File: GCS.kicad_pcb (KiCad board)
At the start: 2 copper layers, 53 parts, among them J1 PROC_EXTAL_GND, J2 USB_B, J3 PA_CON, J4 PB_CON, J5 ASYNC0_OPT, J6 ASYNC0_IO, J7 ASYNC1_OPT, J8 ASYNC1_IO, SW1 SW_Push, U1 MC6809, U10 MC6850, U11 74HCT00, U2 DS1813, U3 MC68B21, U4 HM62256BLP-7, U5 29C256, U6 74LS138, U7 74LS138, U8 MC6850, U9 74LS138, X1 CXO_DIP8, Y1 Crystal

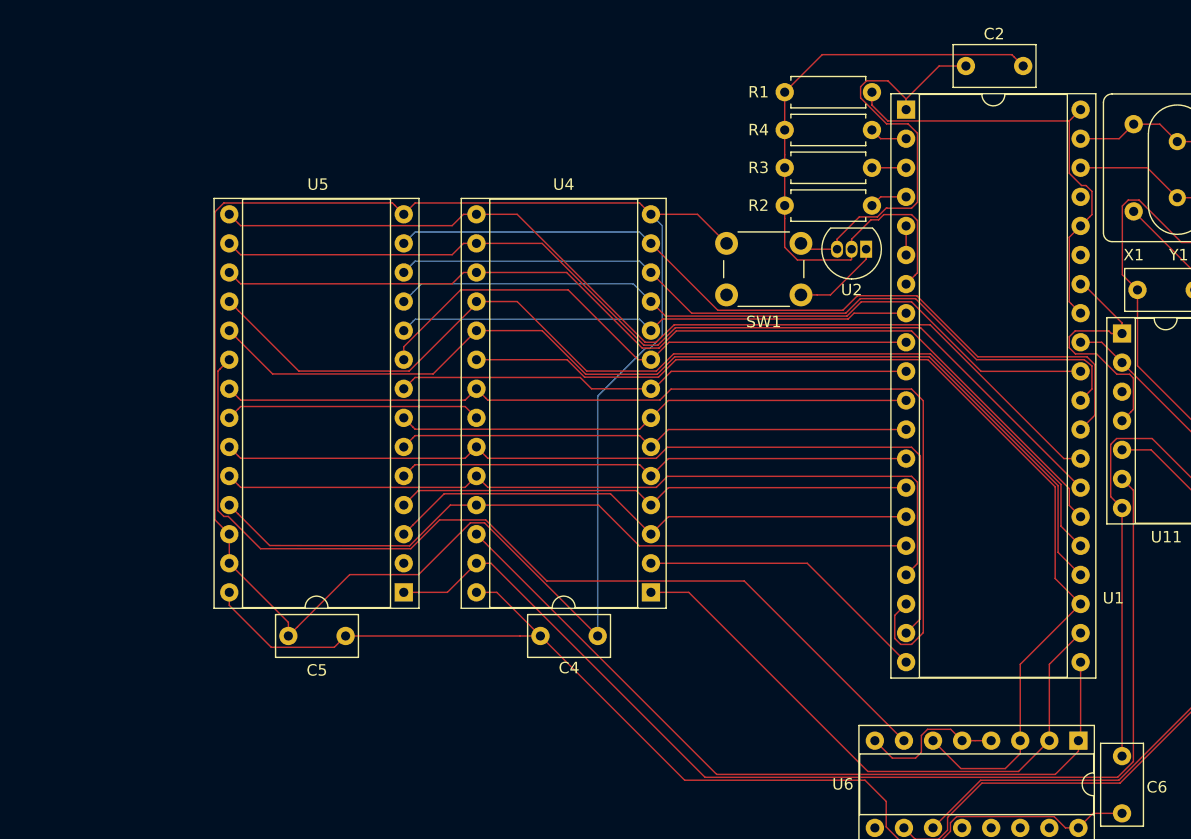
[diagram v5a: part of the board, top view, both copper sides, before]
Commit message: Added header for expandable ram
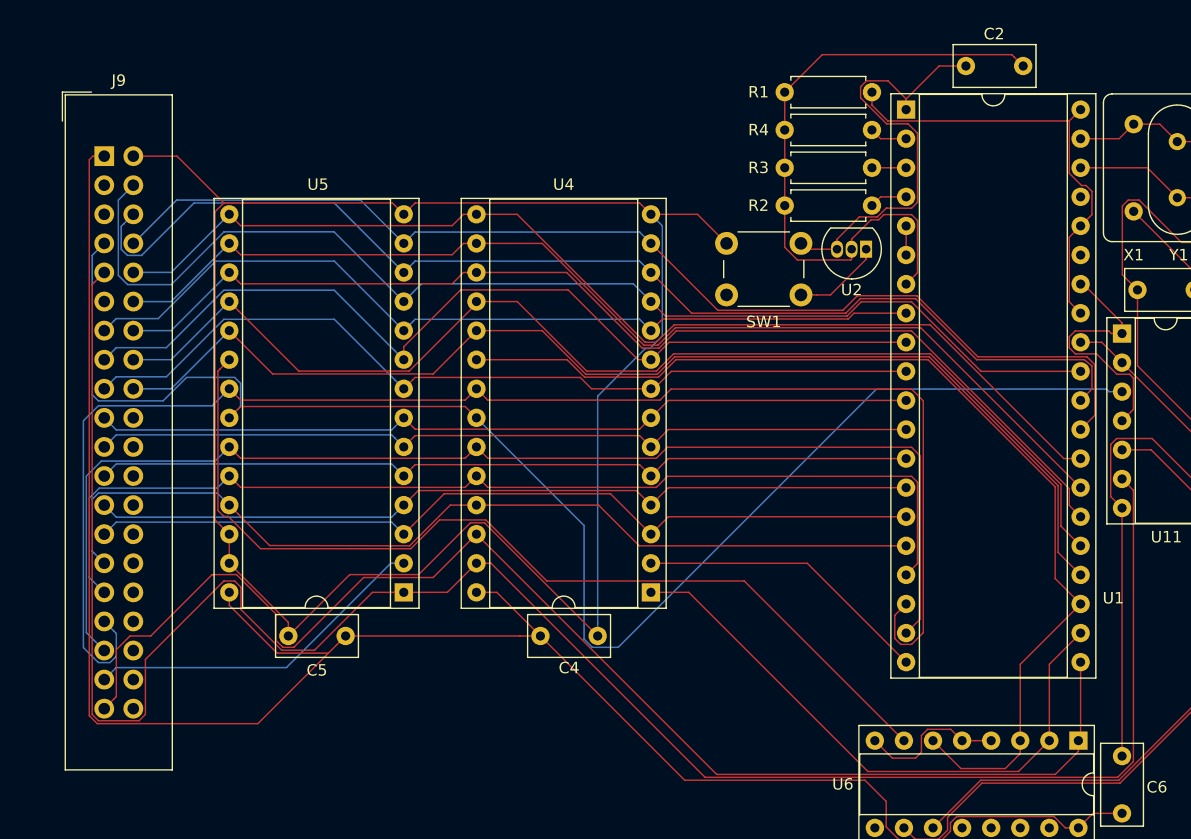
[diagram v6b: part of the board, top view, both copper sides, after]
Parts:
- added J9: Conn_02x20_Odd_Even, Connector_IDC:IDC-Header_2x20_P2.54mm_Vertical, F.Cu at (70.4, 84.3)
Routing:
- net /~R: track 22.4 -> 133.7 mm
- net /~W: track 98.2 -> 178.3 mm
- net VCC: track 169.7 -> 243.9 mm
- net /A13: track 70.0 -> 117.8 mm
- net /A10: track 89.5 -> 130.3 mm
- net /D0: track 64.0 -> 102.1 mm
- net /D1: track 68.8 -> 101.6 mm
- net /A1: track 50.2 -> 81.4 mm
- net /A2: track 45.3 -> 76.5 mm
- net /A0: track 45.3 -> 76.5 mm
- net /A12: track 25.9 -> 56.2 mm
- net /A11: track 78.3 -> 107.7 mm
- net /A7: track 47.4 -> 74.5 mm
- net /A5: track 45.3 -> 72.4 mm
- net /A3: track 45.3 -> 72.4 mm
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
